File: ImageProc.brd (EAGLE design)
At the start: 49.8 x 23.2 mm, 117 parts, among them IC1 XC61GC3002HR-G, IC10 AT45DB642D-CNU, IC2 MIC5335-SPYMT, IC3 MIC5335-JGYMT, IC4 DSPIC33FJ128MC706A, IC5 AT86RF233-ZU, IC6 LTC6088, IC7 DRV8833RTY, IC8 DRV8833RTY, IC9 MPU-6000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

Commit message: Resolved the three wiring issues (non-connect on the v_batt plane, non-connect for a logic ground, and programming connector backwards).
Added the biomimetics dru's
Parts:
- moved C4 2.69 mm to (15.8, 19.4), turned to 180 degrees
- moved C1 0.22 mm to (15.5, 21.1)
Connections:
- net !RESET: now also JP1.5; no longer JP1.1
- net 3.3V: now also JP1.4; no longer JP1.2
- net PGC: now also JP1.1; no longer JP1.5
- net PGD: now also JP1.2; no longer JP1.4
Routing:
- net MOTOR_C_IN2: track 47.5 -> 29.9 mm
- net MOTOR_A_IN1: track 35.9 -> 50.6 mm, vias 2 -> 3
- net MOTOR_A_IN2: track 31.5 -> 45.6 mm, vias 2 -> 3
- net GND: track 9.08 -> 14.7 mm
- net !RESET: track 42.9 -> 48.5 mm, vias 3 -> 4
- net 3.3V: track 63.6 -> 67.3 mm
- net PGC: track 5.58 -> 7.53 mm

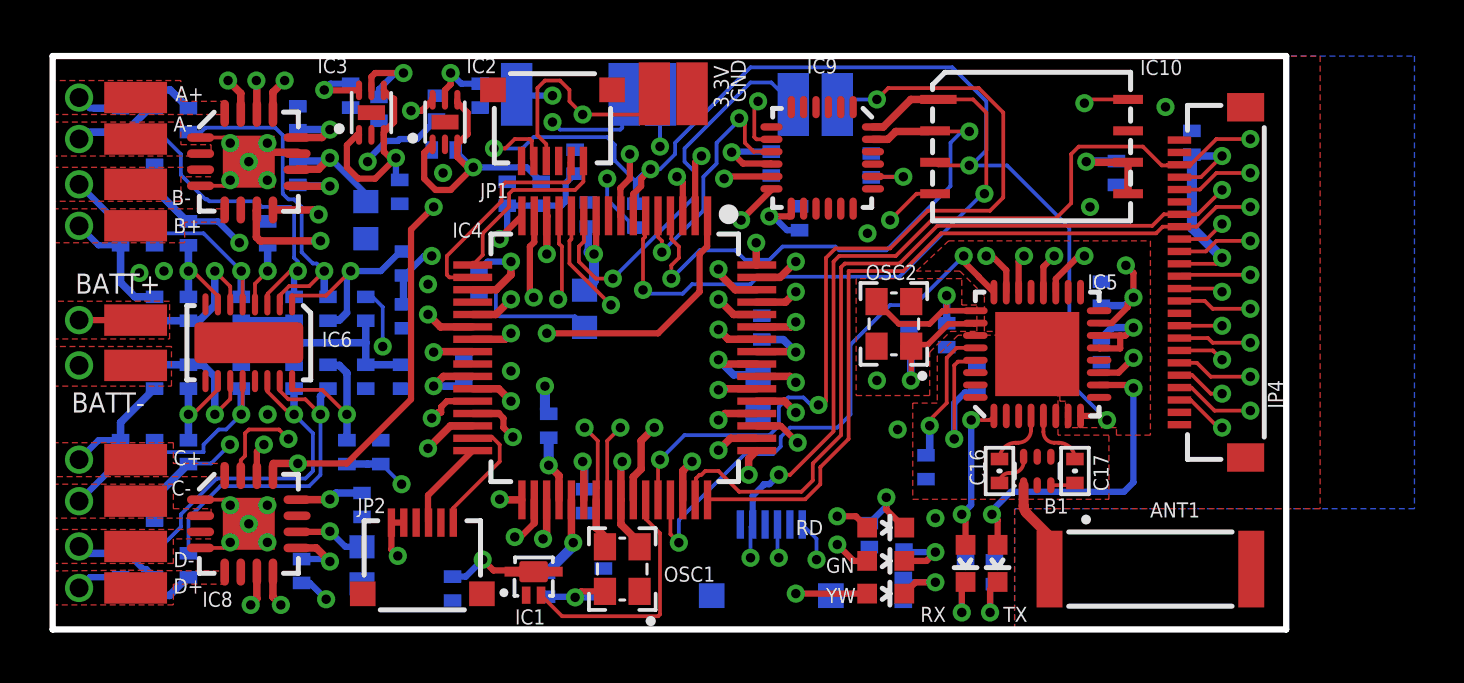
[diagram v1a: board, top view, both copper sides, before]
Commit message: Nudged the outside vias and pads to get sufficient edge clearance.
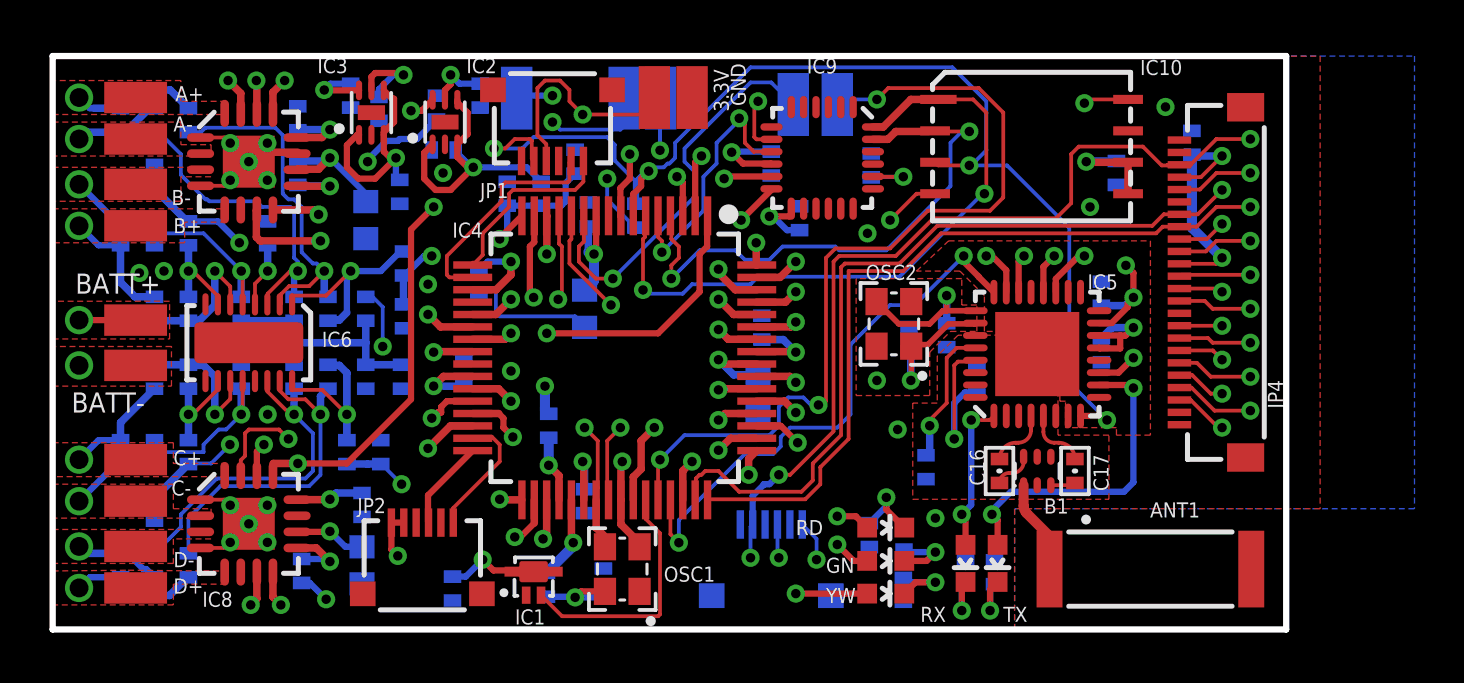
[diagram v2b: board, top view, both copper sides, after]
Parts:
- moved 3.3V 0.15 mm to (24.3, 21.5)
- moved GND 0.15 mm to (25.8, 21.5)
- moved P11 0.15 mm to (18.7, 21.5)
- moved P12 0.15 mm to (23.1, 21.5)
- moved P13 0.15 mm to (24.6, 21.5)
